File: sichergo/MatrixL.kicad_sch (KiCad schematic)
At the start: 36 parts, among them SW1 SW_Push, SW10 SW_Push, SW11 SW_Push, SW12 SW_Push, SW13 SW_Push, SW14 SW_Push, SW15 SW_Push, SW16 SW_Push, SW19 SW_Push, SW20 SW_Push, SW21 SW_Push, SW3 SW_Push, SW4 SW_Push, SW5 SW_Push, SW6 SW_Push, SW7 SW_Push, SW8 SW_Push, SW9 SW_Push

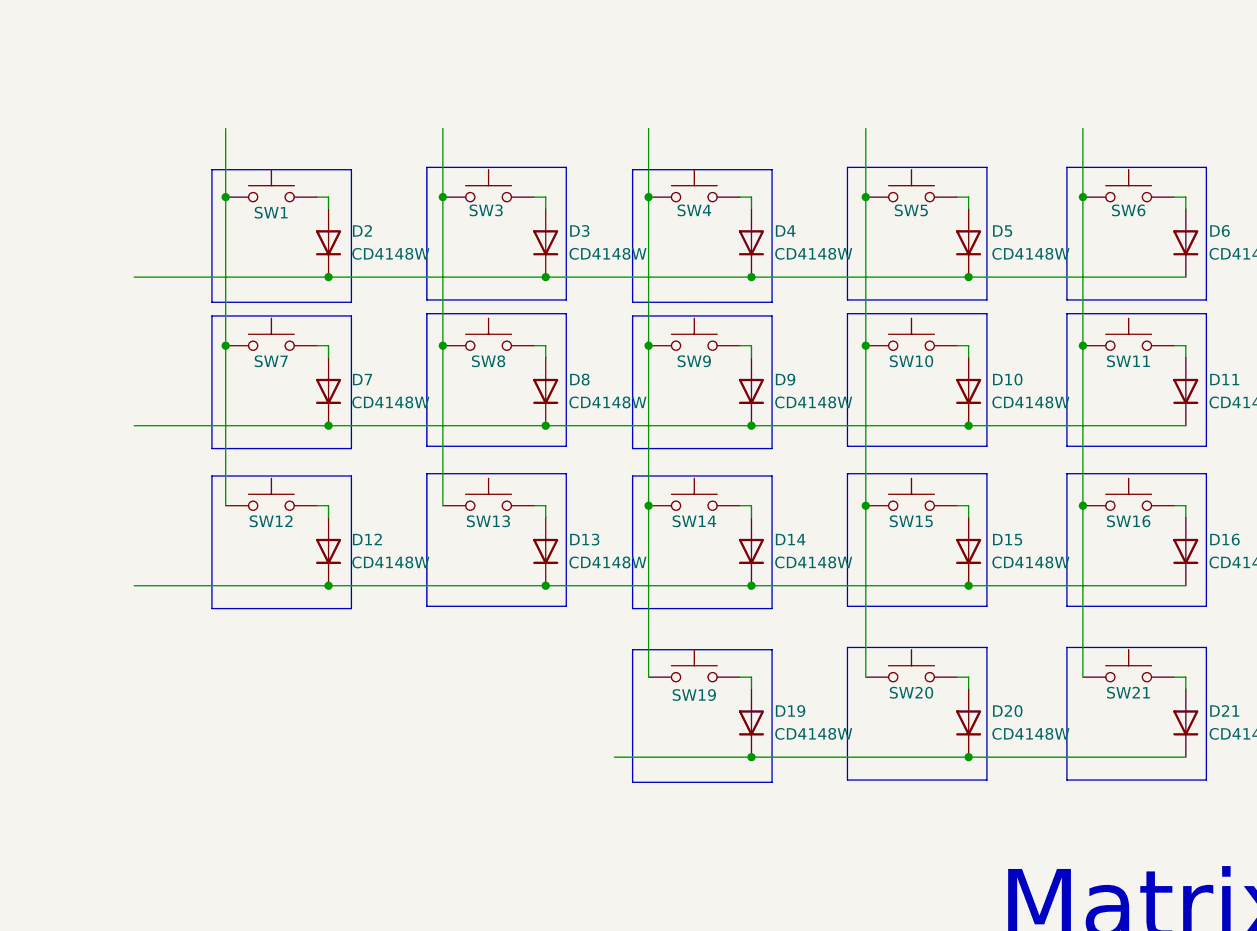
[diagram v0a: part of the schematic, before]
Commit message: Added footprints to switches
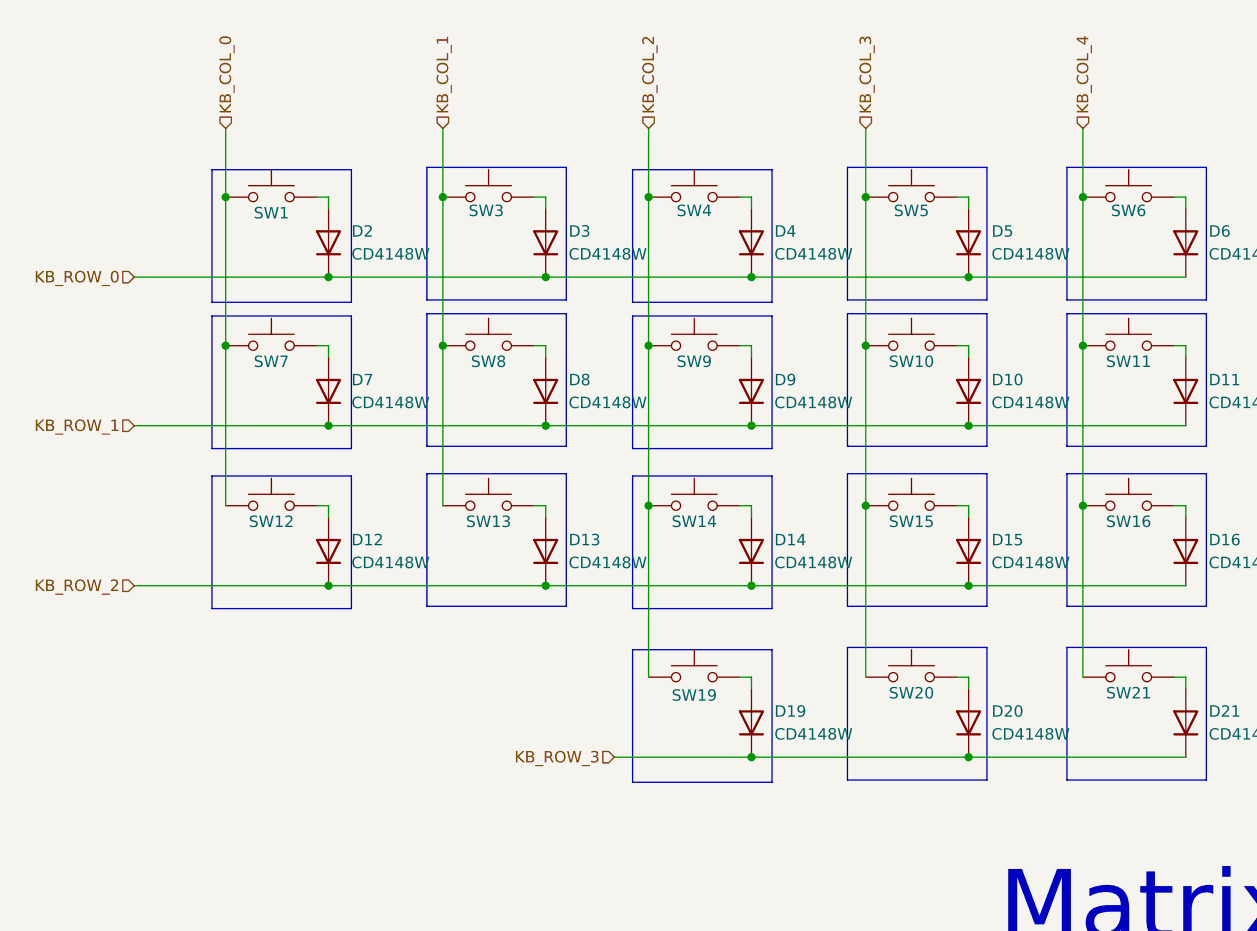
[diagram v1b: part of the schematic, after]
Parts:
- SW1, SW10, SW11, SW12, SW13, SW14, SW15, SW16, SW19, SW20, SW21, SW3, SW4, SW5, SW6, SW7, SW8, SW9: footprint (none) -> personal:Gateron_Milky_Yellow
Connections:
- net KB_ROW_1: now reaches D10.1 (K), D11.1 (K), D7.1 (K), D8.1 (K), D9.1 (K)
- net KB_ROW_0: now reaches D2.1 (K), D3.1 (K), D4.1 (K), D5.1 (K), D6.1 (K)
- net KB_COL_4: now reaches SW11.1, SW16.1, SW21.1, SW6.1
- net KB_COL_1: now reaches SW13.1, SW3.1, SW8.1
- net KB_ROW_3: now reaches D19.1 (K), D20.1 (K), D21.1 (K)
- net KB_COL_2: now reaches SW14.1, SW19.1, SW4.1, SW9.1
- net KB_COL_3: now reaches SW10.1, SW15.1, SW20.1, SW5.1
- net KB_ROW_2: now reaches D12.1 (K), D13.1 (K), D14.1 (K), D15.1 (K), D16.1 (K)
- net KB_COL_0: now reaches SW1.1, SW12.1, SW7.1
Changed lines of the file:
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@@
+		)
+	)
+	(hierarchical_label "KB_ROW_0"
+		(shape input)
+		(at 34.29 41.91 180)
+		(effects
+			(font
+				(size 1.27 1.27)
+			)
+			(justify right)
+		)
+	)
+	(hierarchical_label "KB_COL_3"
+		(shape input)
+		(at 115.57 25.4 90)
+		(effects
+			(font
+				(size 1.27 1.27)
+			)
+			(justify left)
+		)
+	)
+	(hierarchical_label "KB_COL_1"
+		(shape input)
+		(at 68.58 25.4 90)
+		(effects
+			(font
+				(size 1.27 1.27)
+			)
+			(justify left)
+		)
+	)
+	(hierarchical_label "KB_ROW_2"
+		(shape input)
+		(at 34.29 76.2 180)
+		(effects
+			(font
+				(size 1.27 1.27)
+			)
+			(justify right)
+		)
+	)
+	(hierarchical_label "KB_COL_2"
+		(shape input)
+		(at 91.44 25.4 90)
+		(effects
+			(font
+				(size 1.27 1.27)
+			)
+			(justify left)
+		)
+	)
+	(hierarchical_label "KB_COL_0"
+		(shape input)
+		(at 44.45 25.4 90)
+		(effects
+			(font
+				(size 1.27 1.27)
+			)
+			(justify left)
+		)
+	)
+	(hierarchical_label "KB_ROW_3"
+		(shape input)
+		(at 87.63 95.25 180)
+		(effects
+			(font
+				(size 1.27 1.27)
+			)
+			(justify right)
+		)
+	)
+	(hierarchical_label "KB_ROW_1"
+		(shape input)
+		(at 34.29 58.42 180)
+		(effects
+			(font
+				(size 1.27 1.27)
+			)
+			(justify right)
+		)
+	)
+	(hierarchical_label "KB_COL_4"
+		(shape input)
+		(at 139.7 25.4 90)
+		(effects
+			(font
+				(size 1.27 1.27)
+			)
+			(justify left)
 		)
 	)
@@
 			)
 		)
-		(property "Footprint" ""
+		(property "Footprint" "personal:Gateron_Milky_Yellow"
 			(at 144.78 27.94 0)
 			(effects
@@
 			)
 		)
-		(property "Footprint" ""
+		(property "Footprint" "personal:Gateron_Milky_Yellow"
 			(at 73.66 27.94 0)
 			(effects
@@
 			)
 		)
-		(property "Footprint" ""
+		(property "Footprint" "personal:Gateron_Milky_Yellow"
 			(at 96.52 81.28 0)
 			(effects
@@
 			)
 		)
-		(property "Footprint" ""
+		(property "Footprint" "personal:Gateron_Milky_Yellow"
 			(at 144.78 44.45 0)
 			(effects
@@
 			)
 		)
-		(property "Footprint" ""
+		(property "Footprint" "personal:Gateron_Milky_Yellow"
 			(at 120.65 81.28 0)
 			(effects
@@
 			)
 		)
-		(property "Footprint" ""
+		(property "Footprint" "personal:Gateron_Milky_Yellow"
 			(at 96.52 62.23 0)
 			(effects
@@
 			)
 		)
-		(property "Footprint" ""
+		(property "Footprint" "personal:Gateron_Milky_Yellow"
 			(at 120.65 27.94 0)
 			(effects
@@
 			)
 		)
-		(property "Footprint" ""
+		(property "Footprint" "personal:Gateron_Milky_Yellow"
 			(at 49.53 62.23 0)
 			(effects
@@
 			)
 		)
-		(property "Footprint" ""
+		(property "Footprint" "personal:Gateron_Milky_Yellow"
 			(at 96.52 44.45 0)
 			(effects
@@
 			)
 		)
-		(property "Footprint" ""
+		(property "Footprint" "personal:Gateron_Milky_Yellow"
 			(at 120.65 44.45 0)
 			(effects
@@
 			)
 		)
-		(property "Footprint" ""
+		(property "Footprint" "personal:Gateron_Milky_Yellow"
 			(at 96.52 27.94 0)
 			(effects
@@
 			)
 		)
-		(property "Footprint" ""
+		(property "Footprint" "personal:Gateron_Milky_Yellow"
 			(at 49.53 27.94 0)
 			(effects
@@
 			)
 		)
-		(property "Footprint" ""
+		(property "Footprint" "personal:Gateron_Milky_Yellow"
 			(at 73.66 44.45 0)
 			(effects
@@
 			)
 		)
-		(property "Footprint" ""
+		(property "Footprint" "personal:Gateron_Milky_Yellow"
 			(at 73.66 62.23 0)
 			(effects
@@
 			)
 		)
-		(property "Footprint" ""
+		(property "Footprint" "personal:Gateron_Milky_Yellow"
 			(at 120.65 62.23 0)
 			(effects
@@
 			)
 		)
-		(property "Footprint" ""
+		(property "Footprint" "personal:Gateron_Milky_Yellow"
 			(at 144.78 81.28 0)
 			(effects
@@
 			)
 		)
-		(property "Footprint" ""
+		(property "Footprint" "personal:Gateron_Milky_Yellow"
 			(at 49.53 44.45 0)
 			(effects
@@
 			)
 		)
-		(property "Footprint" ""
+		(property "Footprint" "personal:Gateron_Milky_Yellow"
 			(at 144.78 62.23 0)
 			(effects

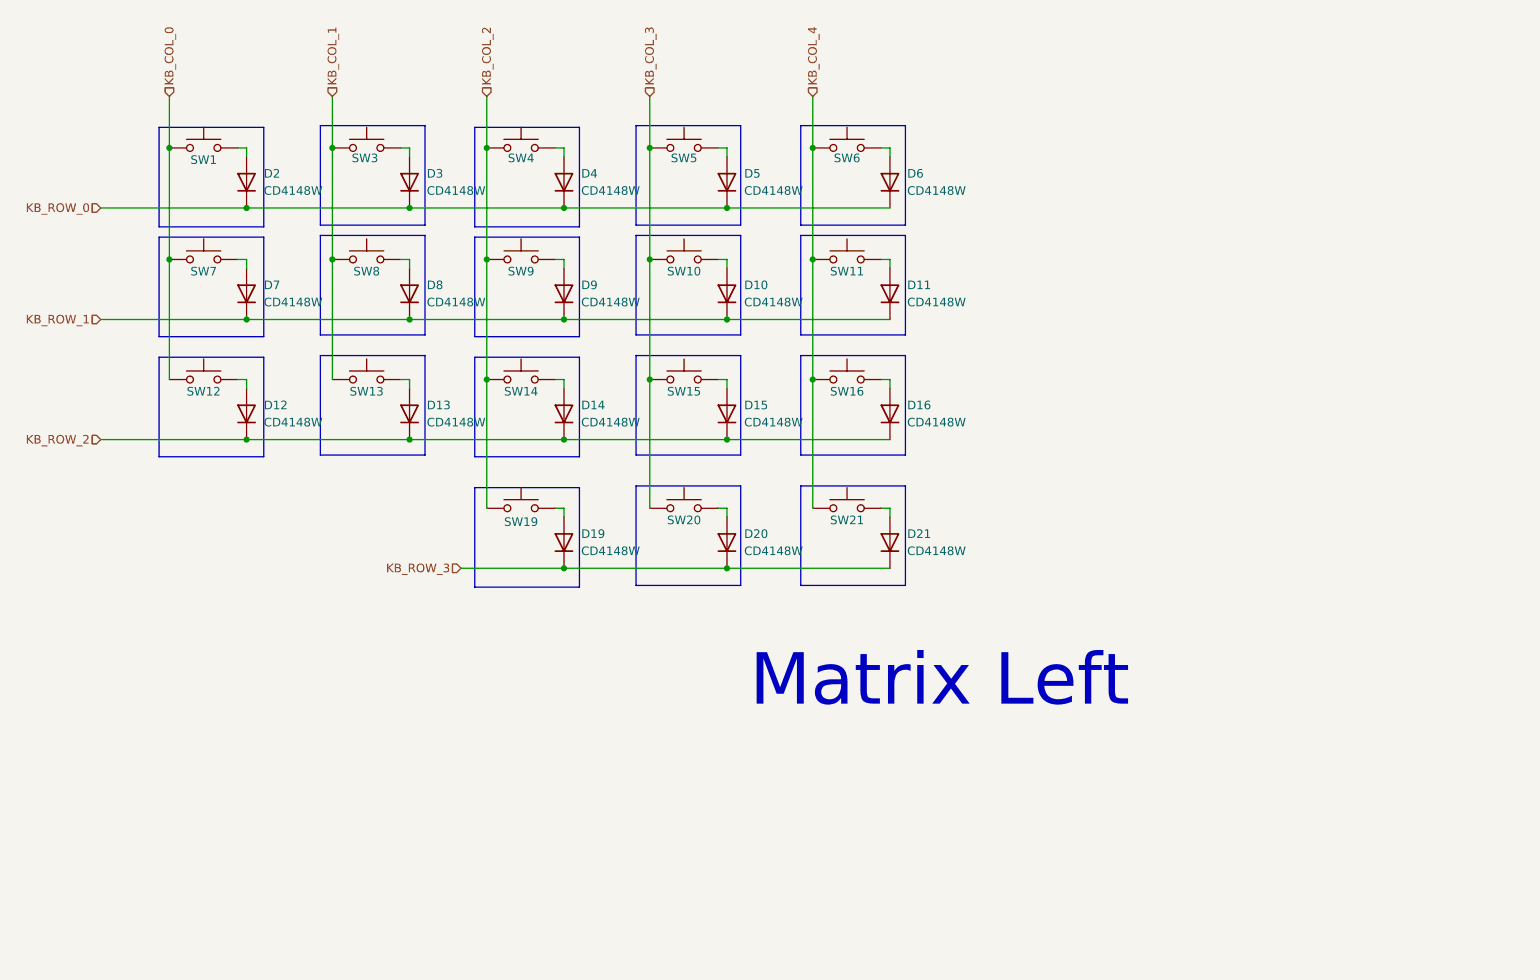
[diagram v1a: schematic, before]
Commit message: Add backlight and switch connections
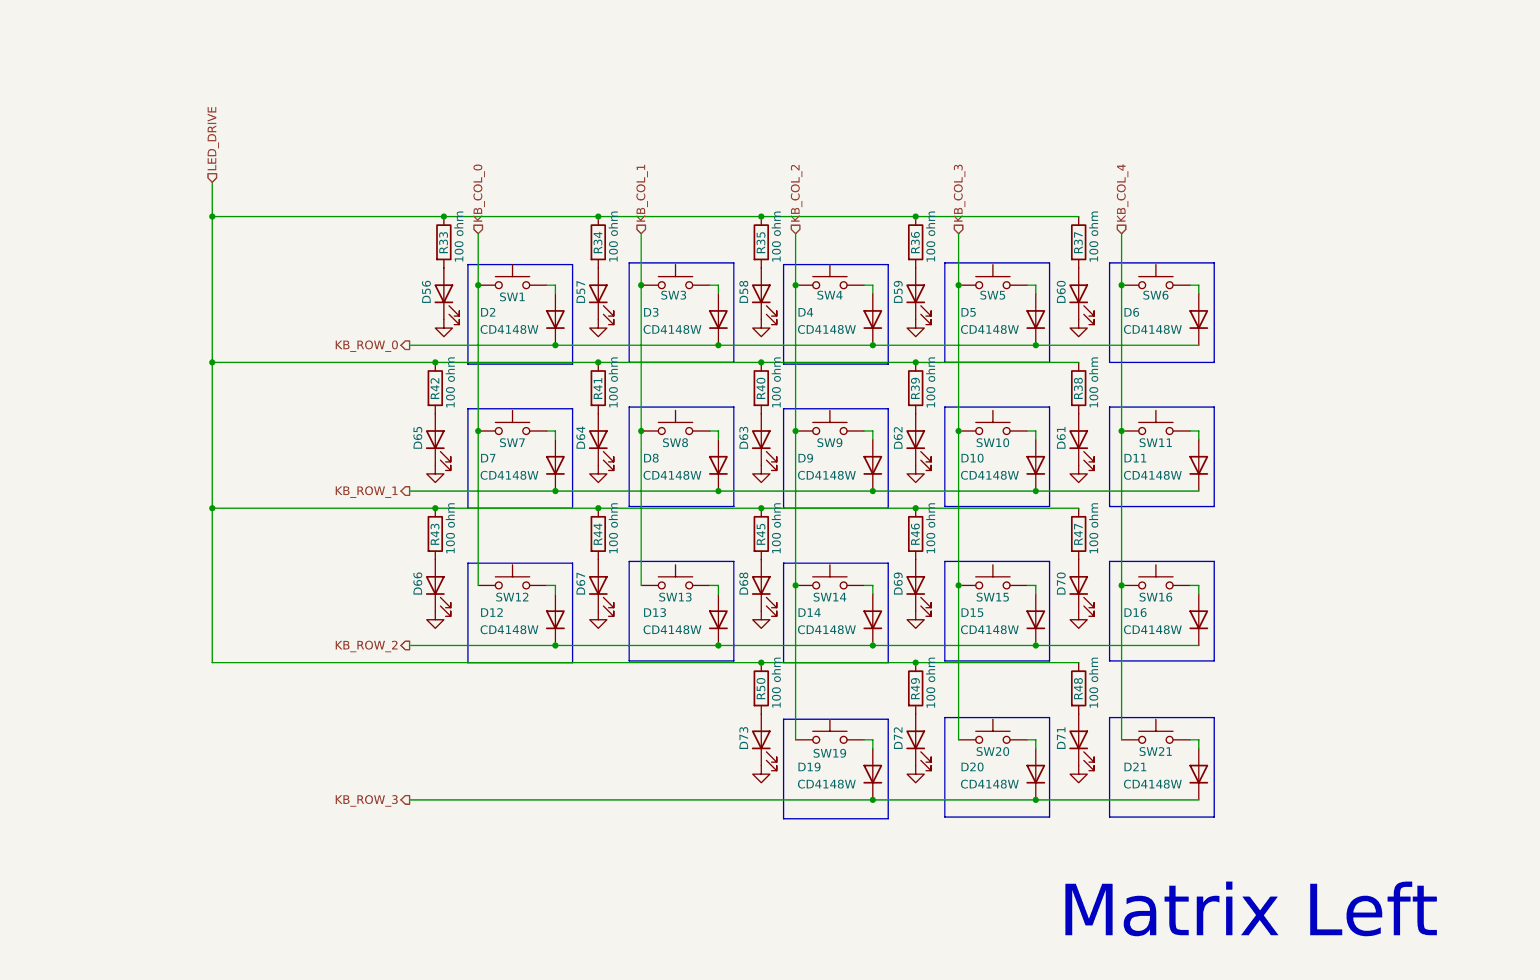
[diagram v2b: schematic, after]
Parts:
- added D56, D57, D58, D59, D60, D61, D62, D63, D64, D65, D66, D67, D68, D69, D70, D71, D72, D73: LED, LED_SMD:LED_0603_1608Metric_Pad1.05x0.95mm_HandSolder, symbol Device:LED
- added R33, R34, R35, R36, R37, R38, R39, R40, R41, R42, R43, R44, R45, R46, R47, R48, R49, R50: 100 ohm, Resistor_SMD:R_0805_2012Metric_Pad1.20x1.40mm_HandSolder, symbol #inventree:ERJ-6GEYJ101V
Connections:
- new net: D70.2 (A), R47.2
- new net: D66.2 (A), R43.2
- new net: D63.2 (A), R40.2
- new net: D68.2 (A), R45.2
- new net: D69.2 (A), R46.2
- new net: D57.2 (A), R34.2
- new net: D58.2 (A), R35.2
- new net: D73.2 (A), R50.2
- new net: D65.2 (A), R42.2
- new net: D61.2 (A), R38.2
- new net: D67.2 (A), R44.2
- new net: D71.2 (A), R48.2
- new net: D62.2 (A), R39.2
- new net: D59.2 (A), R36.2
- new net: D72.2 (A), R49.2
- new net: D56.2 (A), R33.2
- new net: D60.2 (A), R37.2
- new net: D64.2 (A), R41.2
- new net GND: D56.1 (K), D57.1 (K), D58.1 (K), D59.1 (K), D60.1 (K), D61.1 (K), D62.1 (K), D63.1 (K), D64.1 (K), D65.1 (K), D66.1 (K), D67.1 (K), D68.1 (K), D69.1 (K), D70.1 (K), D71.1 (K), D72.1 (K), D73.1 (K)
- new net LED_DRIVE: R33.1, R34.1, R35.1, R36.1, R37.1, R38.1, R39.1, R40.1, R41.1, R42.1, R43.1, R44.1, R45.1, R46.1, R47.1, R48.1, R49.1, R50.1
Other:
- moved on the sheet: D10, D11, D12, D13, D14, D15, D16, D19, D2, D20, D21, D3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

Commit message: Pre finish layout
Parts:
- removed R33, R34, R35, R36, R37, R38, R39, R40, R41, R42, R43, R44, R45, R46, R47, R48, R49, R50: 100 ohm, Resistor_SMD:R_0805_2012Metric_Pad1.20x1.40mm_HandSolder, symbol #inventree:ERJ-6GEYJ101V
- added R33, R34, R35, R36, R37, R38, R39, R40, R41, R42, R43, R44, R45, R46, R47, R48, R49, R50: 1 kohm, Resistor_SMD:R_0603_1608Metric_Pad0.98x0.95mm_HandSolder, symbol #inventree:RC0603FR-071KL
- D56, D57, D58, D59, D60, D61, D62, D63, D64, D65, D66, D67, D68, D69, D70, D71, D72, D73: InvenTree (none) -> 67
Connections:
- net LED_DRIVE: now also R33.1, R34.1, R35.1, R36.1, R37.1, R38.1, R39.1, R40.1, R41.1, R42.1, R43.1, R44.1, R45.1, R46.1, R47.1, R48.1, R49.1, R50.1
- net at D70.2 (A): now also R46.2
- net at D66.2 (A): now also R38.2
- net at D63.2 (A): now also R49.2
- net at D68.2 (A): now also R44.2
- net at D69.2 (A): now also R47.2
- net at D57.2 (A): now also R35.2
- net at D58.2 (A): now also R50.2
- net at D73.2 (A): now also R33.2
- net at D65.2 (A): now also R43.2
- net at D61.2 (A): now also R39.2
- net at D67.2 (A): now also R37.2
- net at D71.2 (A): now also R45.2
- net at D62.2 (A): now also R42.2
- net at D59.2 (A): now also R41.2
- net at D72.2 (A): now also R36.2
- net at D56.2 (A): now also R34.2
- net at D60.2 (A): now also R40.2
- net at D64.2 (A): now also R48.2
